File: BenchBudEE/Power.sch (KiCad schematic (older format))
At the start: 13 parts, among them P1 CONN_12X2, SW1 SWITCH_INV

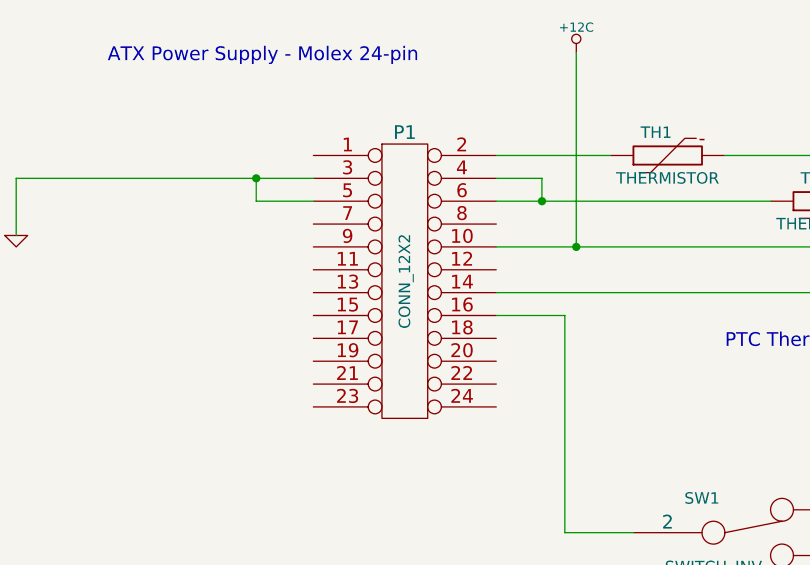
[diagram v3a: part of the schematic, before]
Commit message: Associated the Terminal/ATX block components.
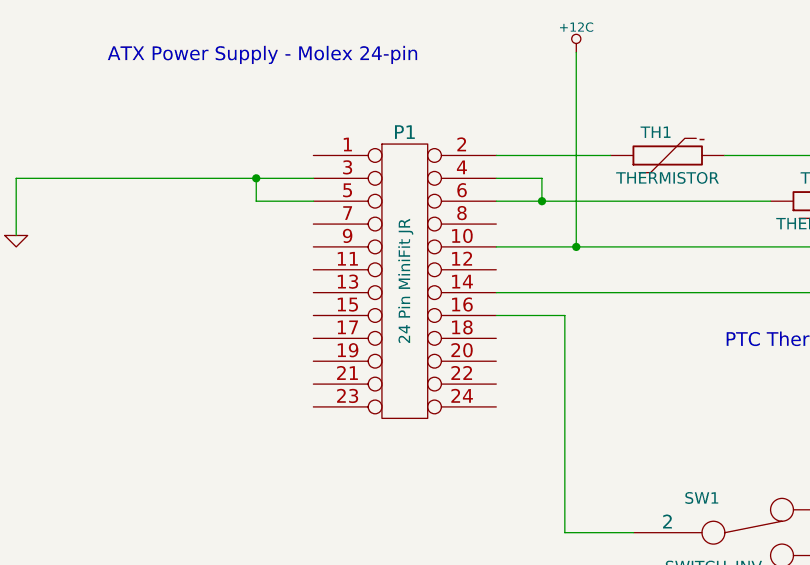
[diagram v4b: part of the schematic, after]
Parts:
- P1: value CONN_12X2 -> 24 Pin MiniFit JR; MFG Name (none) -> Molex; MFG Part Number (none) -> 39-30-1240
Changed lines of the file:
@@
 Sheet 4 9
 Title ""
-Date "21 feb 2014"
+Date "22 feb 2014"
 Rev ""
 Comp ""
@@
 P 2550 2050
 F 0 "P1" H 2550 2700 60  0000 C CNN
-F 1 "CONN_12X2" V 2550 2050 50  0000 C CNN
+F 1 "24 Pin MiniFit JR" V 2550 2050 50  0000 C CNN
 F 2 "" H 2550 2050 60  0000 C CNN
 F 3 "" H 2550 2050 60  0000 C CNN
+F 4 "Molex" H 2550 2050 60  0001 C CNN "MFG Name"
+F 5 "39-30-1240" H 2550 2050 60  0001 C CNN "MFG Part Number"
 	1    2550 2050
 	1    0    0    -1

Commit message: Associated components for the Power Protection and Filtering module.
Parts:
- L1, L2, L3: value INDUCTOR -> CM322522-220KL; MFG Name (none) -> Bournes Inc; MFG Part Number (none) -> CM322522-220KL
- SW1: value SWITCH_INV -> Power Switch; MFG Name (none) -> C & K Components; MFG Part Number (none) -> OS102011MA1QN1
- TH1, TH2, TH3, TH4: value THERMISTOR -> MINISMDC050F-2; MFG Name (none) -> TE Connectivity; MFG Part Number (none) -> MINISMDC050F-2
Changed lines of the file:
@@
 P 9550 5300
 F 0 "L1" V 9500 5300 40  0000 C CNN
-F 1 "INDUCTOR" V 9650 5300 40  0000 C CNN
+F 1 "CM322522-220KL" V 9650 5300 40  0000 C CNN
 F 2 "~" H 9550 5300 60  0000 C CNN
 F 3 "~" H 9550 5300 60  0000 C CNN
+F 4 "Bournes Inc" H 9550 5300 60  0001 C CNN "MFG Name"
+F 5 "CM322522-220KL" H 9550 5300 60  0001 C CNN "MFG Part Number"
 	1    9550 5300
 	0    -1   1    0
@@
 P 9600 3900
 F 0 "L2" V 9550 3900 40  0000 C CNN
-F 1 "INDUCTOR" V 9700 3900 40  0000 C CNN
+F 1 "CM322522-220KL" V 9700 3900 40  0000 C CNN
 F 2 "~" H 9600 3900 60  0000 C CNN
 F 3 "~" H 9600 3900 60  0000 C CNN
+F 4 "Bournes Inc" H 9600 3900 60  0001 C CNN "MFG Name"
+F 5 "CM322522-220KL" H 9600 3900 60  0001 C CNN "MFG Part Number"
 	1    9600 3900
 	0    -1   -1   0
@@
 P 4050 3150
 F 0 "SW1" H 3850 3300 50  0000 C CNN
-F 1 "SWITCH_INV" H 3900 3000 50  0000 C CNN
+F 1 "Power Switch" H 3900 3000 50  0000 C CNN
 F 2 "~" H 4050 3150 60  0000 C CNN
 F 3 "~" H 4050 3150 60  0000 C CNN
+F 4 "C & K Components" H 4050 3150 60  0001 C CNN "MFG Name"
+F 5 "OS102011MA1QN1" H 4050 3150 60  0001 C CNN "MFG Part Number"
 	1    4050 3150
 	1    0    0    -1
@@
 P 3700 1500
 F 0 "TH1" V 3800 1550 50  0000 C CNN
-F 1 "THERMISTOR" V 3600 1500 50  0000 C CNN
+F 1 "MINISMDC050F-2" V 3600 1500 50  0000 C CNN
 F 2 "~" H 3700 1500 60  0000 C CNN
 F 3 "~" H 3700 1500 60  0000 C CNN
+F 4 "TE Connectivity" H 3700 1500 60  0001 C CNN "MFG Name"
+F 5 "MINISMDC050F-2" H 3700 1500 60  0001 C CNN "MFG Part Number"
 	1    3700 1500
 	0    -1   -1   0
@@
 P 4400 1700
 F 0 "TH2" V 4500 1750 50  0000 C CNN
-F 1 "THERMISTOR" V 4300 1700 50  0000 C CNN
+F 1 "MINISMDC050F-2" V 4300 1700 50  0000 C CNN
 F 2 "~" H 4400 1700 60  0000 C CNN
 F 3 "~" H 4400 1700 60  0000 C CNN
+F 4 "TE Connectivity" H 4400 1700 60  0001 C CNN "MFG Name"
+F 5 "MINISMDC050F-2" H 4400 1700 60  0001 C CNN "MFG Part Number"
 	1    4400 1700
 	0    -1   -1   0
@@
 P 5150 1900
 F 0 "TH3" V 5250 1950 50  0000 C CNN
-F 1 "THERMISTOR" V 5050 1900 50  0000 C CNN
+F 1 "MINISMDC050F-2" V 5050 1900 50  0000 C CNN
 F 2 "~" H 5150 1900 60  0000 C CNN
 F 3 "~" H 5150 1900 60  0000 C CNN
+F 4 "TE Connectivity" H 5150 1900 60  0001 C CNN "MFG Name"
+F 5 "MINISMDC050F-2" H 5150 1900 60  0001 C CNN "MFG Part Number"
 	1    5150 1900
 	0    -1   -1   0
@@
 P 5700 2100
 F 0 "TH4" V 5800 2150 50  0000 C CNN
-F 1 "THERMISTOR" V 5600 2100 50  0000 C CNN
+F 1 "MINISMDC050F-2" V 5600 2100 50  0000 C CNN
 F 2 "~" H 5700 2100 60  0000 C CNN
 F 3 "~" H 5700 2100 60  0000 C CNN
+F 4 "TE Connectivity" H 5700 2100 60  0001 C CNN "MFG Name"
+F 5 "MINISMDC050F-2" H 5700 2100 60  0001 C CNN "MFG Part Number"
 	1    5700 2100
 	0    -1   -1   0
@@
 P 9650 2000
 F 0 "L3" V 9600 2000 40  0000 C CNN
-F 1 "INDUCTOR" V 9750 2000 40  0000 C CNN
+F 1 "CM322522-220KL" V 9750 2000 40  0000 C CNN
 F 2 "~" H 9650 2000 60  0000 C CNN
 F 3 "~" H 9650 2000 60  0000 C CNN
+F 4 "Bournes Inc" H 9650 2000 60  0001 C CNN "MFG Name"
+F 5 "CM322522-220KL" H 9650 2000 60  0001 C CNN "MFG Part Number"
 	1    9650 2000
 	0    -1   -1   0
